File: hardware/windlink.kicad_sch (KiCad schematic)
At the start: 27 parts, among them J1 M12A-05PMMR-SF7003, J2 61300411121, SW1 EVP-AWCD4A, SW2 EVP-AWCD4A, U1 AP63203WU-7, U2 PTCAN3413DR, U3 ESP32-C6-MINI-1/U

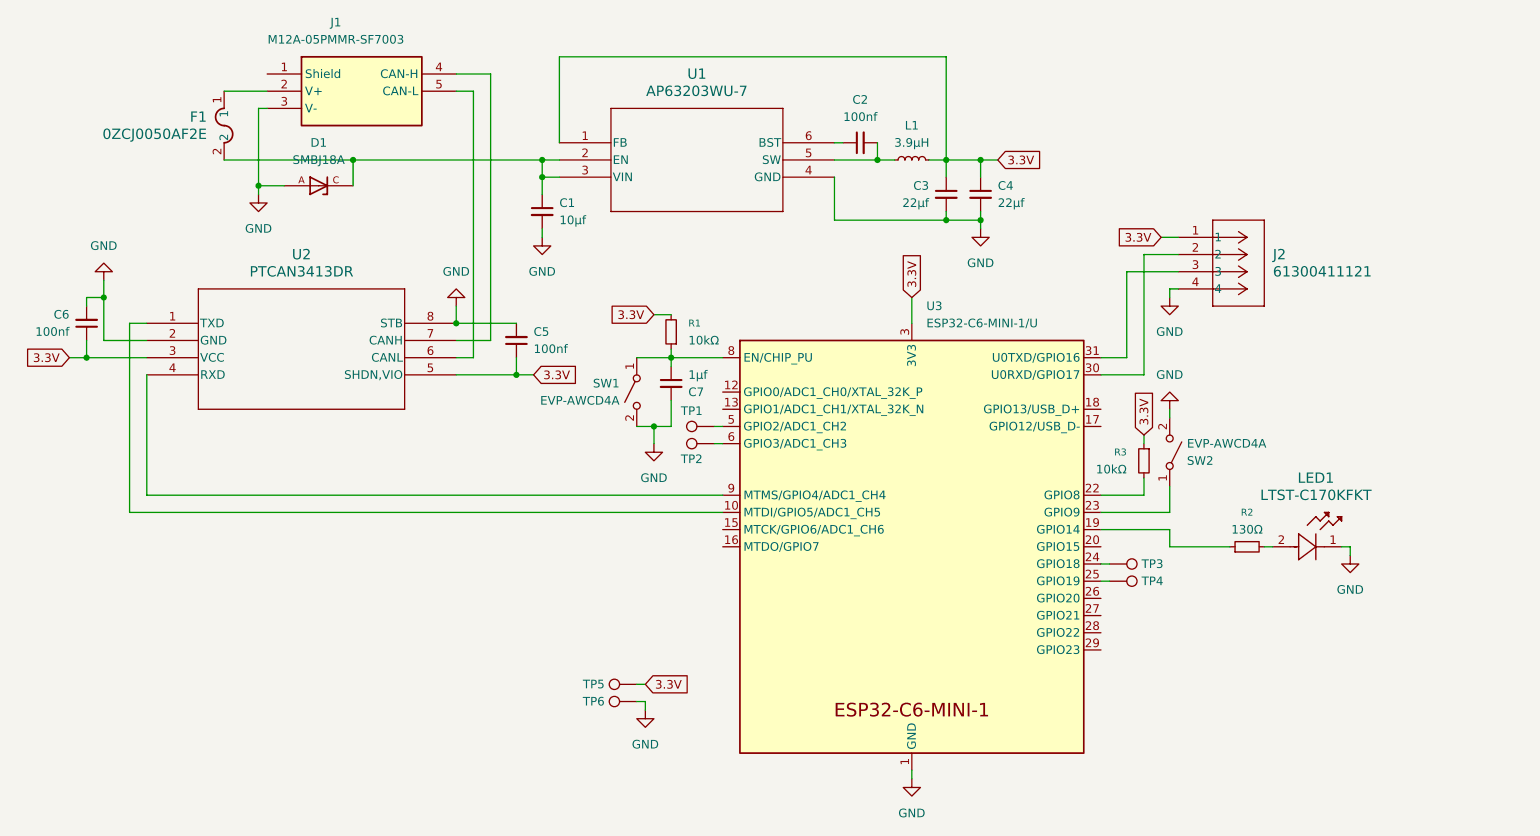
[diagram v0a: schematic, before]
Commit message: PCB: Add extra flash and antenna cutout
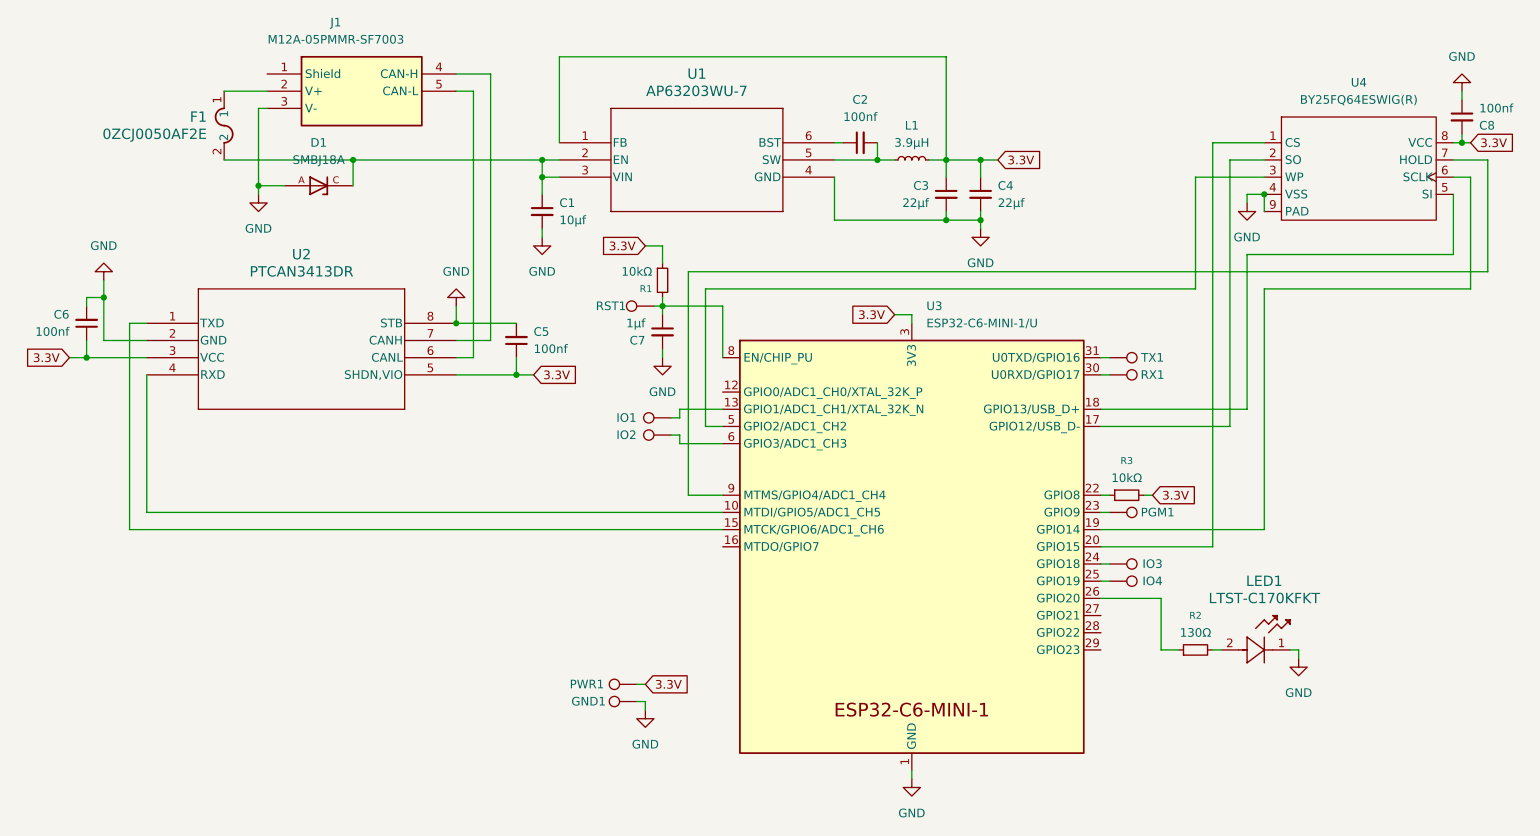
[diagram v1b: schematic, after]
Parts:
- removed J2: 61300411121, 61300411121:CONN_61300411121_WRE, symbol 61300411121:61300411121
- removed SW1, SW2: EVP-AWCD4A, EVP_AWCD4A:SW_EVP-AWCD4A, symbol Switch:SW_SPST
- added C8: 100nf, Capacitor_SMD:C_0805_2012Metric_Pad1.18x1.45mm_HandSolder, symbol Device:C_Small
- added PGM1, RST1, RX1, TX1: TestPoint, TestPoint:TestPoint_Pad_D2.0mm, symbol Connector:TestPoint
- added U4: BY25FQ64ESWIG(R), BY25FQ64ESWIG(R):BY25FQ64ESWIG(R), symbol New_Library:BY25FQ64ESWIG(R)
- renumbered TP6 to GND1, TP1 to IO1, TP2 to IO2, TP3 to IO3, TP4 to IO4, TP5 to PWR1
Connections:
- net 3.3V: now also R1.1, R3.2, C8.2, U4.8 (VCC); no longer R1.2, R3.1
- net GND: now also C8.1, U4.4 (VSS), U4.9 (PAD)
- net at C7.1, U3.8 (EN/CHIP_PU): now also R1.2, RST1.1; no longer R1.1
- net at U3.23 (GPIO9): now also PGM1.1
- net at R2.1: now also U3.26 (GPIO20); no longer U3.19 (GPIO14)
- net at U2.1 (TXD): now also U3.15 (MTCK/GPIO6/ADC1_CH6); no longer U3.10 (MTDI/GPIO5/ADC1_CH5)
- net at U2.4 (RXD): now also U3.10 (MTDI/GPIO5/ADC1_CH5); no longer U3.9 (MTMS/GPIO4/ADC1_CH4)
- net at U3.30 (U0RXD/GPIO17): now also RX1.1
- net at U3.31 (U0TXD/GPIO16): now also TX1.1
- net at IO1.1: now also U3.13 (GPIO1/ADC1_CH1/XTAL_32K_N); no longer U3.5 (GPIO2/ADC1_CH2)
- net at U3.17 (GPIO12/USB_D-): now also U4.2 (SO)
- net at U3.18 (GPIO13/USB_D+): now also U4.5 (SI)
- net at U3.20 (GPIO15): now also U4.1 (CS)
- net at U3.22 (GPIO8): now also R3.1; no longer R3.2
- new net: U3.19 (GPIO14), U4.6 (SCLK)
- new net: U3.5 (GPIO2/ADC1_CH2), U4.3 (WP)
- new net: U3.9 (MTMS/GPIO4/ADC1_CH4), U4.7 (HOLD)
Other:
- moved on the sheet: C7, IO1, IO2, LED1, R1, R2, R3
